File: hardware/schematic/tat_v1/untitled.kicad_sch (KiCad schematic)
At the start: 2 parts, among them J2 USB_C_Receptacle_USB2.0_14P, U6 nPM1300-QEXX

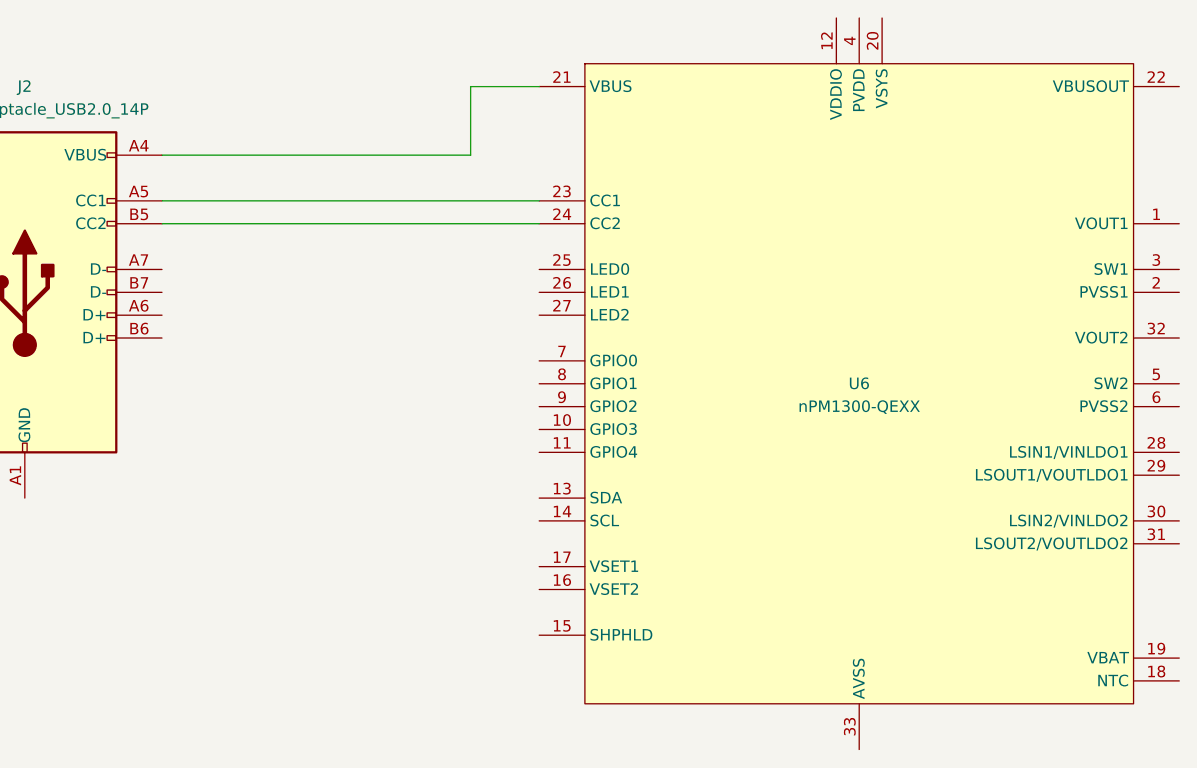
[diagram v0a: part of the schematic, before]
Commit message: Simplified partslist and working on updated schematic
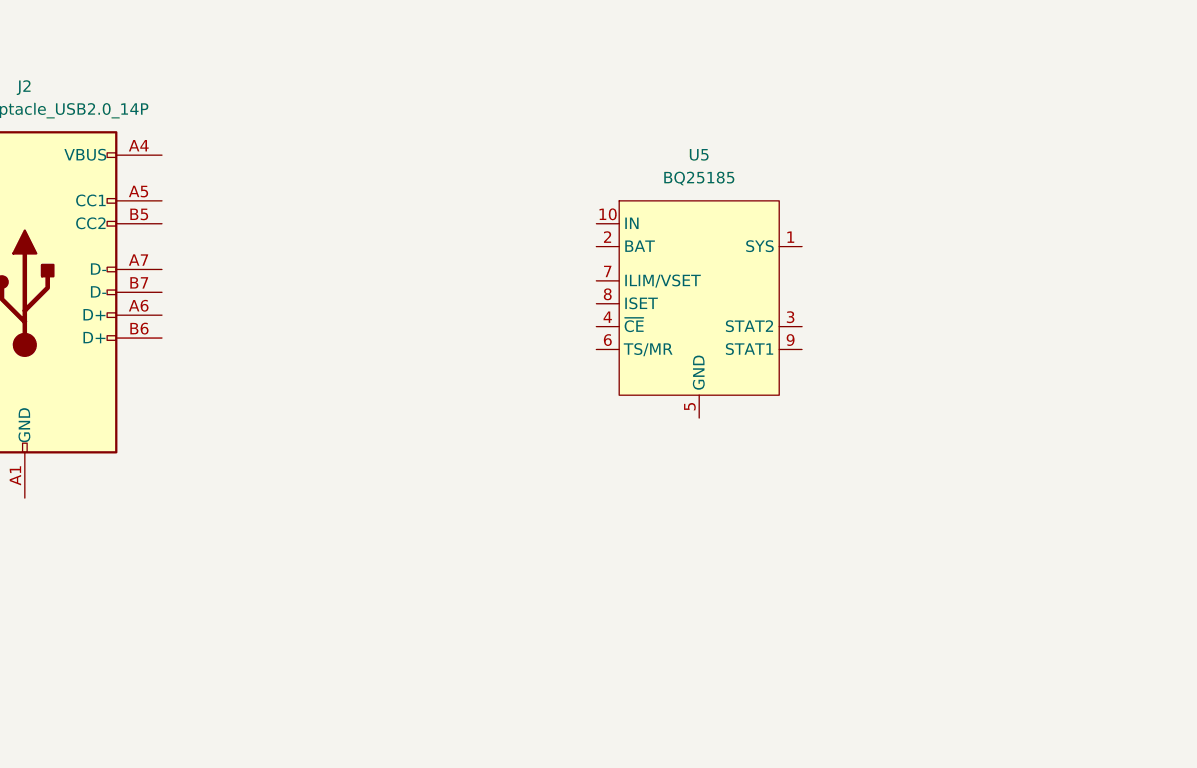
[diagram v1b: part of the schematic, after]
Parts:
- removed U6: nPM1300-QEXX, Package_DFN_QFN:QFN-32-1EP_5x5mm_P0.5mm_EP3.6x3.6mm_ThermalVias, symbol PCM_nordic-lib-kicad-npm:nPM1300-QEXX
- added U5: BQ25185, symbol tat_library:BQ25185
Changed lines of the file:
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@@
 	(generator_version "9.0")
 	(paper "A4")
-	(wire
-		(pts
-			(xy 63.5 83.82) (xy 97.79 83.82)
-		)
-		(stroke
-			(width 0)
-			(type default)
-		)
-	)
-	(wire
-		(pts
-			(xy 63.5 88.9) (xy 105.41 88.9)
-		)
-		(stroke
-			(width 0)
-			(type default)
-		)
-	)
-	(wire
-		(pts
-			(xy 63.5 91.44) (xy 105.41 91.44)
-		)
-		(stroke
-			(width 0)
-			(type default)
-		)
-	)
-	(wire
-		(pts
-			(xy 97.79 76.2) (xy 105.41 76.2)
-		)
-		(stroke
-			(width 0)
-			(type default)
-		)
-	)
-	(wire
-		(pts
-			(xy 97.79 83.82) (xy 97.79 76.2)
-		)
-		(stroke
-			(width 0)
-			(type default)
-		)
-	)
 	(symbol
-		(lib_id "PCM_nordic-lib-kicad-npm:nPM1300-QEXX")
-		(at 140.97 109.22 0)
+		(lib_id "tat_library:BQ25185")
+		(at 123.19 99.06 0)
 		(unit 1)
 		(exclude_from_sim no)
@@
 		(dnp no)
 		(fields_autoplaced yes)
-		(property "Reference" "U6"
-			(at 140.97 109.22 0)
-			(do_not_autoplace yes)
+		(property "Reference" "U5"
+			(at 123.19 83.82 0)
 			(effects
 				(font
@@
 			)
 		)
-		(property "Value" "nPM1300-QEXX"
-			(at 140.97 111.76 0)
-			(do_not_autoplace yes)
+		(property "Value" "BQ25185"
+			(at 123.19 86.36 0)
 			(effects
 				(font
@@
 			)
 		)
-		(property "Footprint" "Package_DFN_QFN:QFN-32-1EP_5x5mm_P0.5mm_EP3.6x3.6mm_ThermalVias"
-			(at 140.97 167.64 0)
+		(property "Footprint" ""
+			(at 123.19 99.06 0)
 			(effects
 				(font
@@
 			)
 		)
-		(property "Datasheet" "https://docs.nordicsemi.com/bundle/ps_npm1300"
-			(at 140.97 165.1 0)
+		(property "Datasheet" ""
+			(at 123.19 99.06 0)
 			(effects
 				(font
@@
 			)
 		)
-		(property "Description" "PMIC, LED Driver, Battery Charger, QFN-32"
-			(at 140.97 162.56 0)
+		(property "Description" ""
+			(at 123.19 99.06 0)
 			(effects
 				(font
@@
 			)
 		)
-		(pin "10"
+		(pin "6"
 		)
-		(pin "24"
+		(pin "9"
 		)
 		(pin "7"
 		)
-		(pin "17"
-		)
-		(pin "23"
-		)
-		(pin "27"
-		)
-		(pin "25"
-		)
-		(pin "21"
-		)
-		(pin "26"
+		(pin "4"
 		)
 		(pin "8"
 		)
-		(pin "9"
-		)
-		(pin "11"
-		)
-		(pin "13"
-		)
-		(pin "14"
-		)
-		(pin "29"
-		)
-		(pin "20"
-		)
-		(pin "12"
-		)
-		(pin "15"
-		)
-		(pin "33"
-		)
-		(pin "4"
-		)
-		(pin "31"
-		)
-		(pin "28"
-		)
-		(pin "6"
-		)
-		(pin "22"
-		)
-		(pin "18"
-		)
-		(pin "3"
+		(pin "10"
 		)
 		(pin "5"
@@
 		(pin "1"
 		)
-		(pin "16"
-		)
-		(pin "32"
-		)
-		(pin "19"
-		)
 		(pin "2"
 		)
-		(pin "30"
+		(pin "3"
 		)
 		(instances
 			(project ""
 				(path "/b6d2ddf1-6792-45dd-afc9-29fd74d587ec/5056535a-bc75-42d4-a05e-c6bbb85e2678"
-					(reference "U6")
+					(reference "U5")
 					(unit 1)
 				)

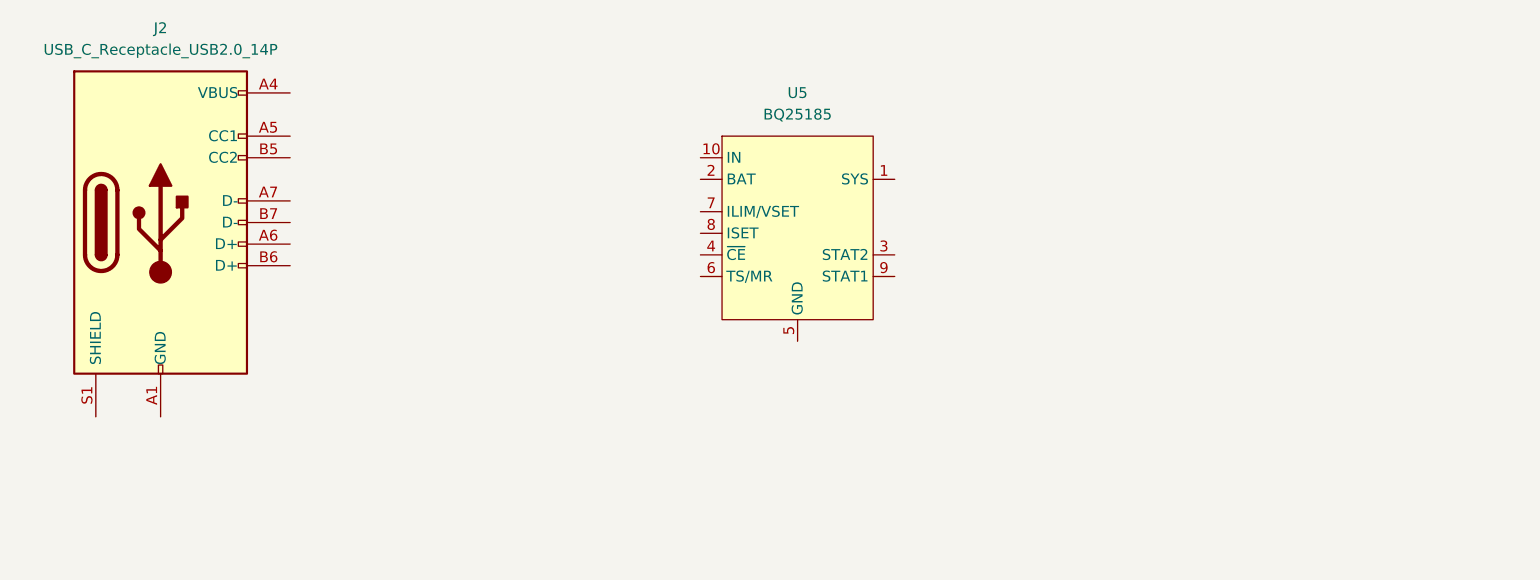
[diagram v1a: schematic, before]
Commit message: Added some parts, working on USB and power inputs
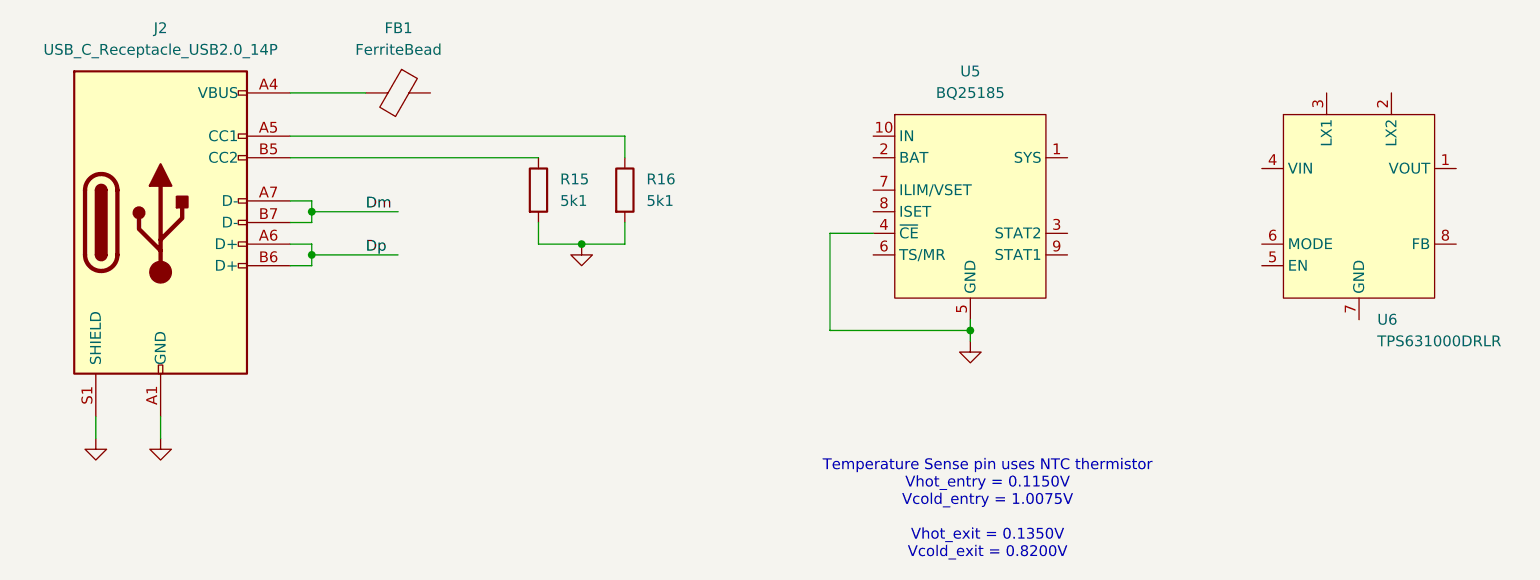
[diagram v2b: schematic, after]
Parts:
- added FB1: FerriteBead, symbol Device:FerriteBead
- added R15, R16: 5k1, symbol Device:R
- added U6: TPS631000DRLR, symbol tat_library:TPS631000DRLR
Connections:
- net GND: now reaches U5.4 (~{CE})
- net GND: now also J2.A1 (GND), J2.A12 (GND), J2.B1 (GND), J2.B12 (GND), J2.S1 (SHIELD), U5.5 (GND), R15.2, R16.2
- net at J2.A4 (VBUS), J2.A9 (VBUS), J2.B4 (VBUS)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: now also FB1.2
- net at J2.A5 (CC1): now also R16.1
- net Dp: now reaches J2.A6 (D+)
- net Dp: now also J2.B6 (D+)
- net Dm: now reaches J2.A7 (D-)
- net Dm: now also J2.B7 (D-)
- net at J2.B5 (CC2): now also R15.1
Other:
- note added: "Temperature Sense pin uses NTC thermistor Vhot_entry = 0.1150V Vcold_entry = 1.0075V Vhot_exit = 0.1350V Vcold_exit = 0.8200V"
- moved on the sheet: U5

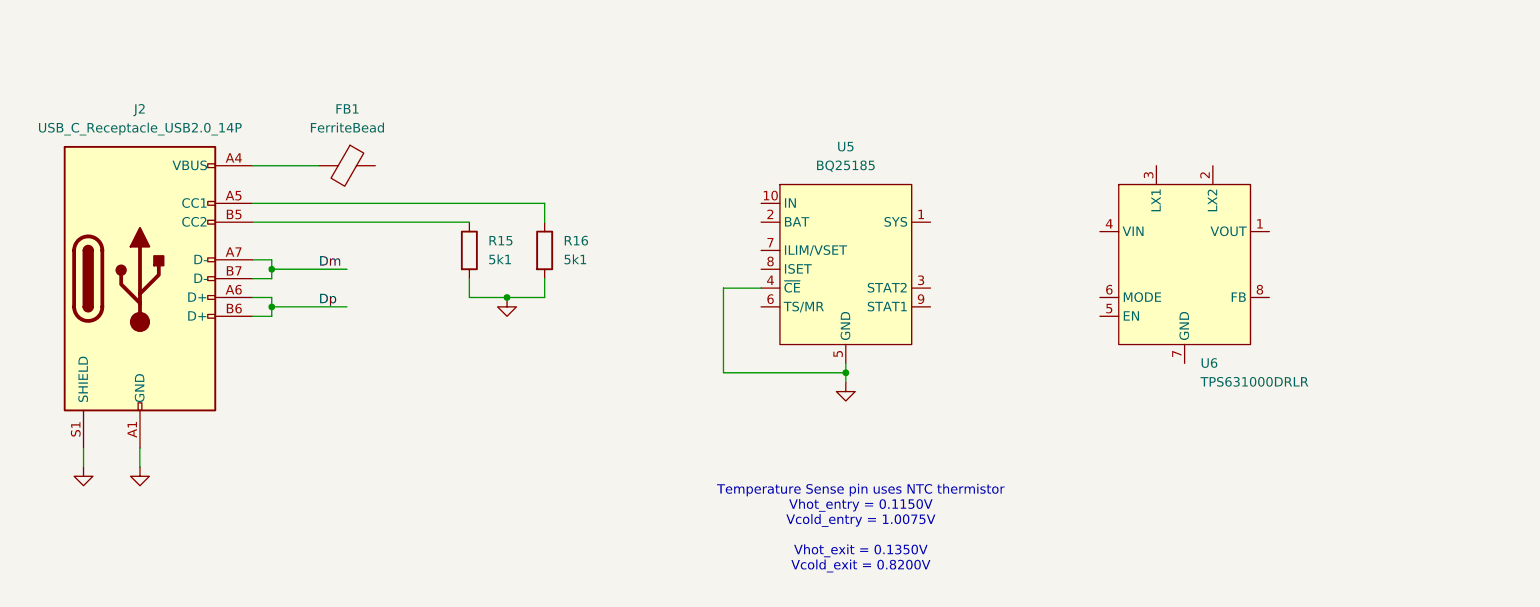
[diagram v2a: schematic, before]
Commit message: Working on power schematic
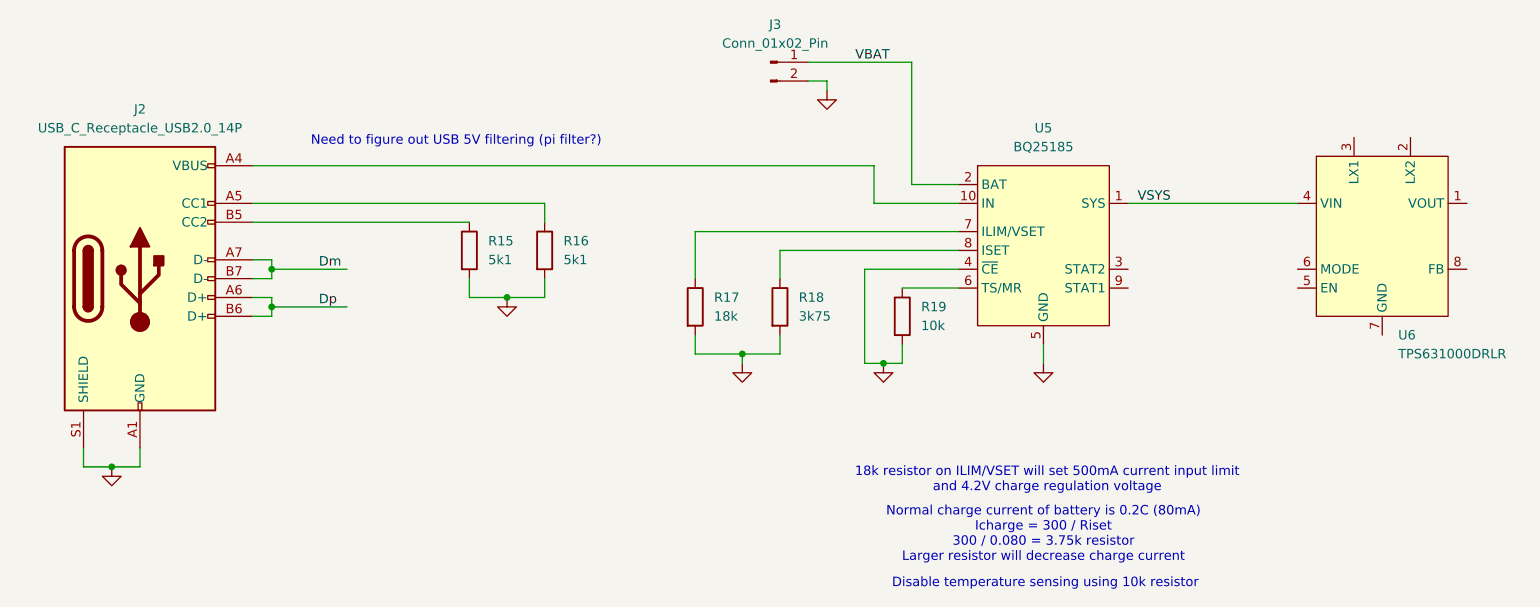
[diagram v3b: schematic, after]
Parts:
- removed FB1: FerriteBead, symbol Device:FerriteBead
- added J3: Conn_01x02_Pin, symbol Connector:Conn_01x02_Pin
- added R17: 18k, symbol Device:R
- added R18: 3k75, symbol Device:R
- added R19: 10k, symbol Device:R
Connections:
- net GND: now also J3.2 (Pin_2), R17.2, R18.2, R19.2
- net VSYS: now reaches U6.4 (VIN)
- net VSYS: now also U5.1 (SYS)
- net at U5.10 (IN): now also J2.A4 (VBUS), J2.A9 (VBUS), J2.B4 (VBUS), J2.B9 (VBUS)
- net VBAT: now reaches U5.2 (BAT)
- net VBAT: now also J3.1 (Pin_1)
- net at U5.6 (TS/MR): now also R19.1
- net at U5.7 (ILIM/VSET): now also R17.1
- net at U5.8 (ISET): now also R18.1
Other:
- note added: "18k resistor on ILIM/VSET will set 500mA current input limit and 4.2V charge regulation voltage"
- note added: "Disable temperature sensing using 10k resistor"
- note added: "Need to figure out USB 5V filtering (pi filter?)"
- note added: "Normal charge current of battery is 0.2C (80mA) Icharge = 300 / Riset 300 / 0.080 = 3.75k resistor Larger resistor will decrease charge current"
- note removed: "Temperature Sense pin uses NTC thermistor Vhot_entry = 0.1150V Vcold_entry = 1.0075V Vhot_exit = 0.1350V Vcold_exit = 0.8200V"
- moved on the sheet: U5, U6

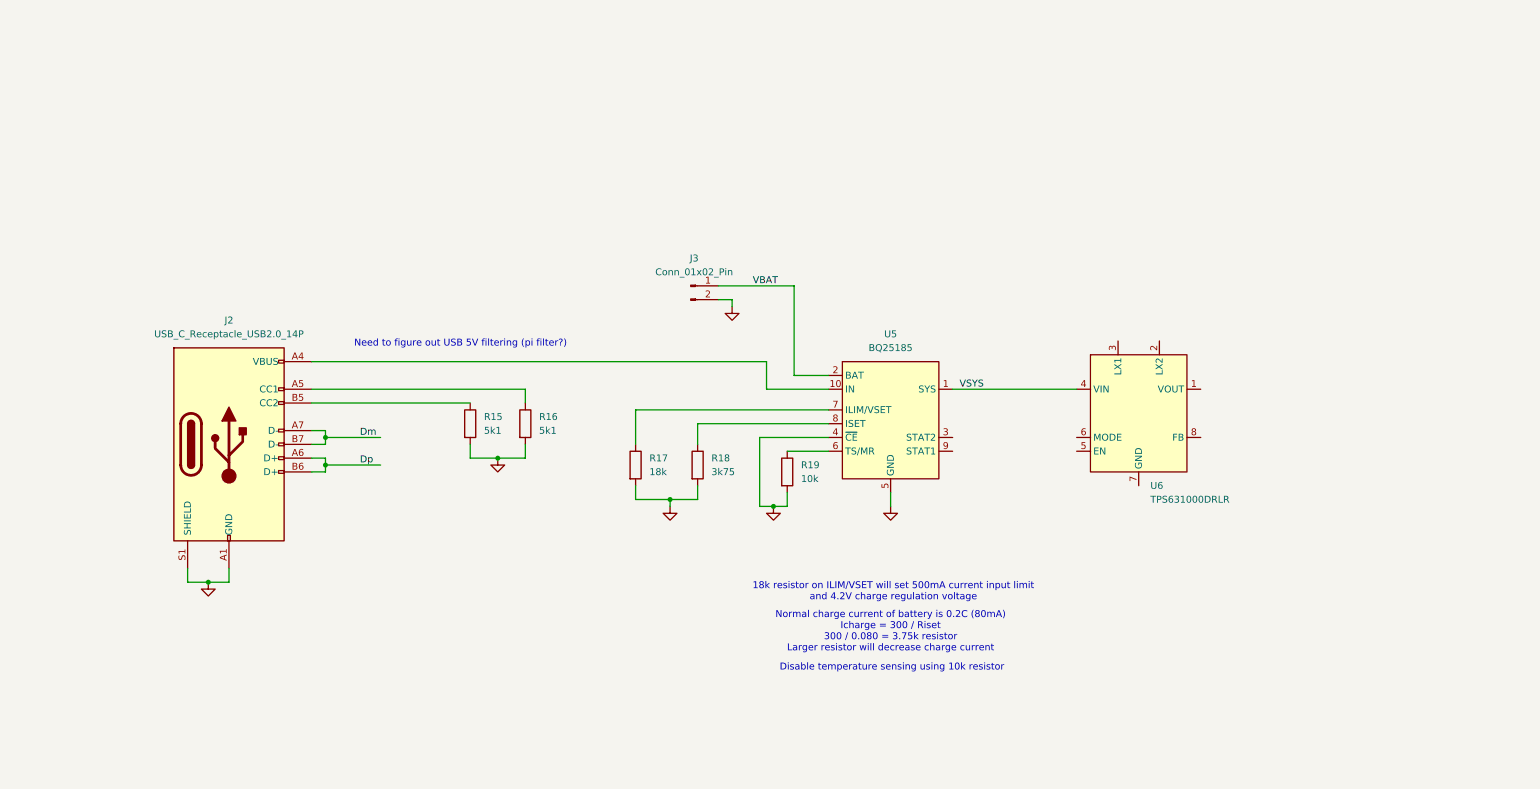
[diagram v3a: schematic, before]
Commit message: Added small details to power sheet. Added PXRD's ferrite to partslist for reference
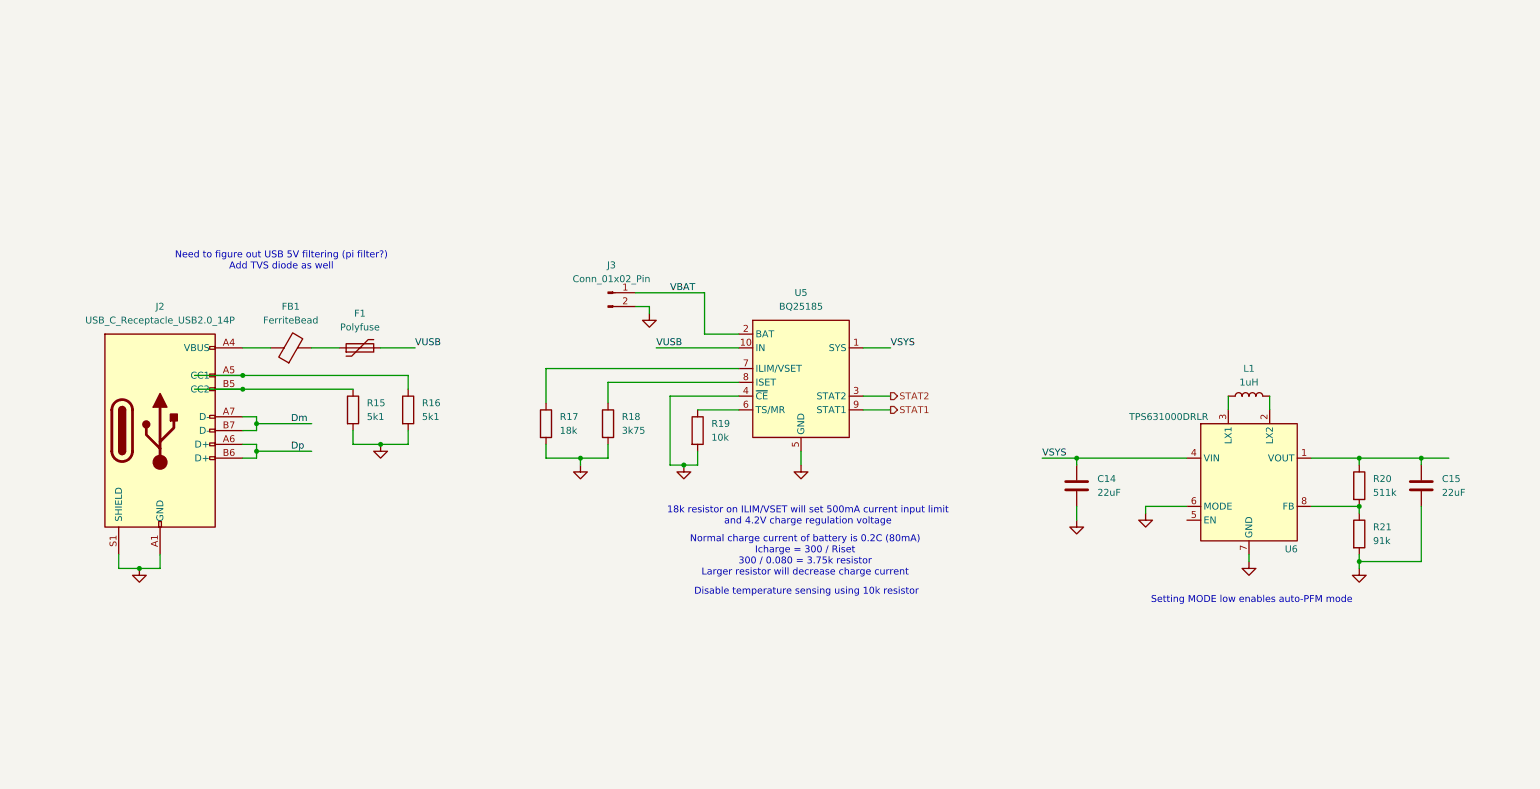
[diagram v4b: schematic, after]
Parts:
- added C14, C15: 22uF, symbol Device:C
- added F1: Polyfuse, symbol Device:Polyfuse
- added FB1: FerriteBead, symbol Device:FerriteBead
- added L1: 1uH, symbol Device:L
- added R20: 511k, symbol Device:R
- added R21: 91k, symbol Device:R
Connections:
- net GND: now also U6.6 (MODE), U6.7 (GND), C14.2, C15.2, R21.2
- net VSYS: now also C14.1
- net at U6.1 (VOUT): now also C15.1, R20.1
- net at U6.2 (LX2): now also L1.2
- net at U6.3 (LX1): now also L1.1
- net at U6.8 (FB): now also R20.2, R21.1
- net at J2.A4 (VBUS), J2.A9 (VBUS), J2.B4 (VBUS)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: now also FB1.1; no longer U5.10 (IN)
- net STAT2: now reaches U5.3 (STAT2)
- net STAT1: now reaches U5.9 (STAT1)
- new net: F1.1, FB1.2
- new net VUSB: F1.2, U5.10 (IN)
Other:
- note added: "Need to figure out USB 5V filtering (pi filter?) Add TVS diode as well"
- note added: "Setting MODE low enables auto-PFM mode"
- note removed: "Need to figure out USB 5V filtering (pi filter?)"
- moved on the sheet: J2, J3, R15, R16, R17, R18, R19, U5, U6
